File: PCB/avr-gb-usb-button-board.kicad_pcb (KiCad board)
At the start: 2 copper layers, 81 x 51.1 mm, 28 parts, among them IC1 ATTINY88-A

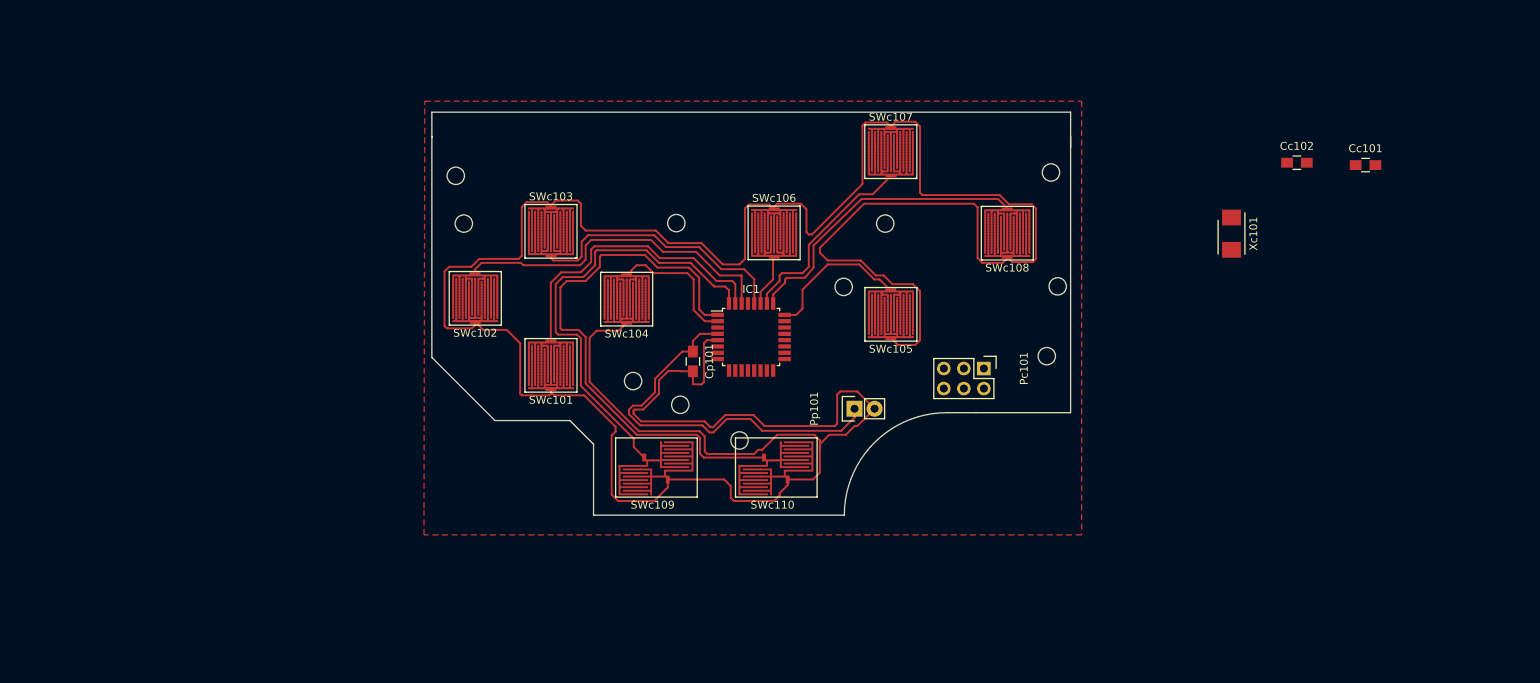
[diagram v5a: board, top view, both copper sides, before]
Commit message: Wired ISP header
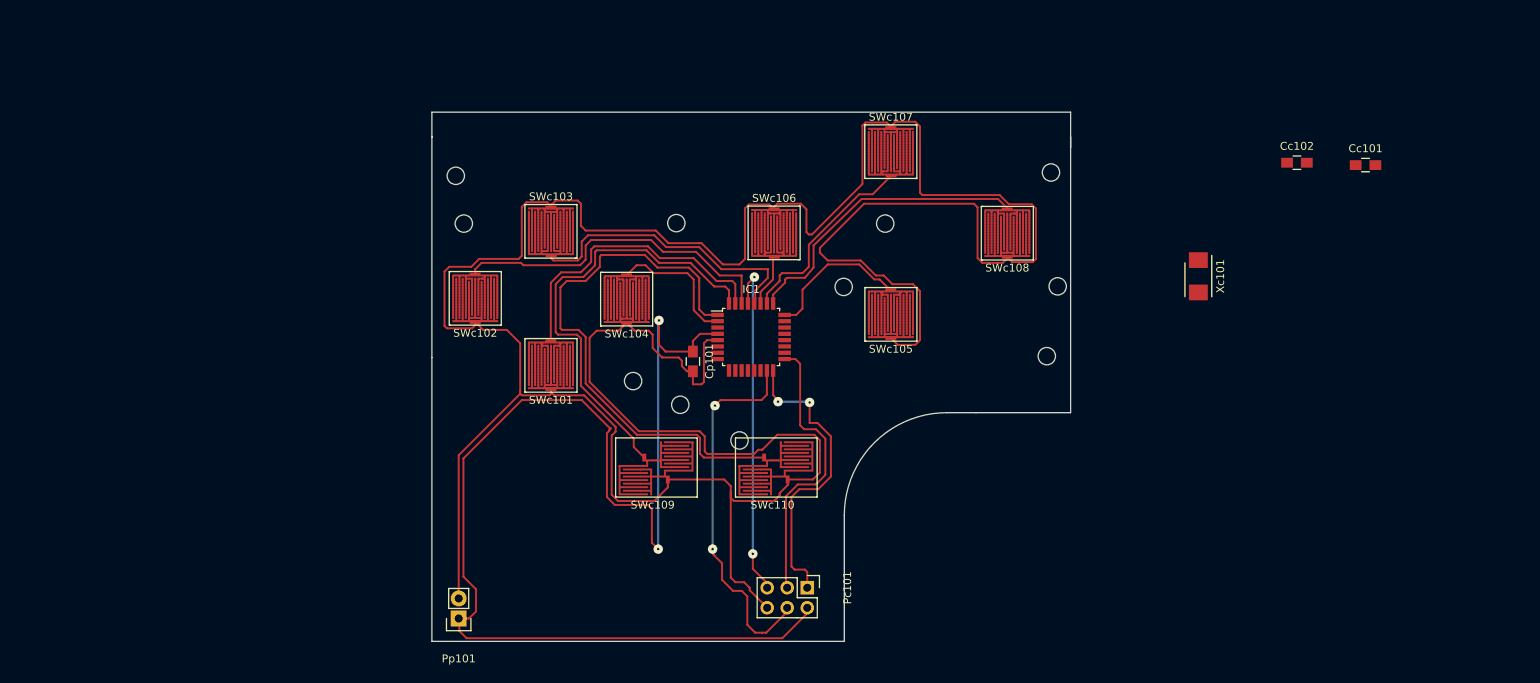
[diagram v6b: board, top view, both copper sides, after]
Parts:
- moved Pp101 56.8 mm to (22.8, 82.3), turned to 180 degrees
- moved Pc101 35.7 mm to (67.0, 78.4)
- moved Xc101 6.84 mm to (116.6, 38.9)
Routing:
- net VCC: track 50.3 -> 155.6 mm, vias 0 -> 2
- net Net-(IC1-Pad15): track 0.00 -> 47.7 mm, vias 0 -> 2
- net Net-(IC1-Pad29): track 0.00 -> 43.9 mm, vias 0 -> 2
- net Net-(IC1-Pad16): track 0.00 -> 38.5 mm, vias 0 -> 2
- net Net-(IC1-Pad17): track 0.00 -> 36.3 mm
- net Net-(IC1-Pad28): track 34.1 -> 37.3 mm
- net GND: track 389.2 -> 390.1 mm
- removed copper zone on F.Cu, net GND
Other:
- board size 81 x 51.1 mm -> 81 x 67.1 mm
- net class Default: via_dia 0.6 -> 1.2; via_drill 0.4 -> 0.3

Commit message: Added oscillator
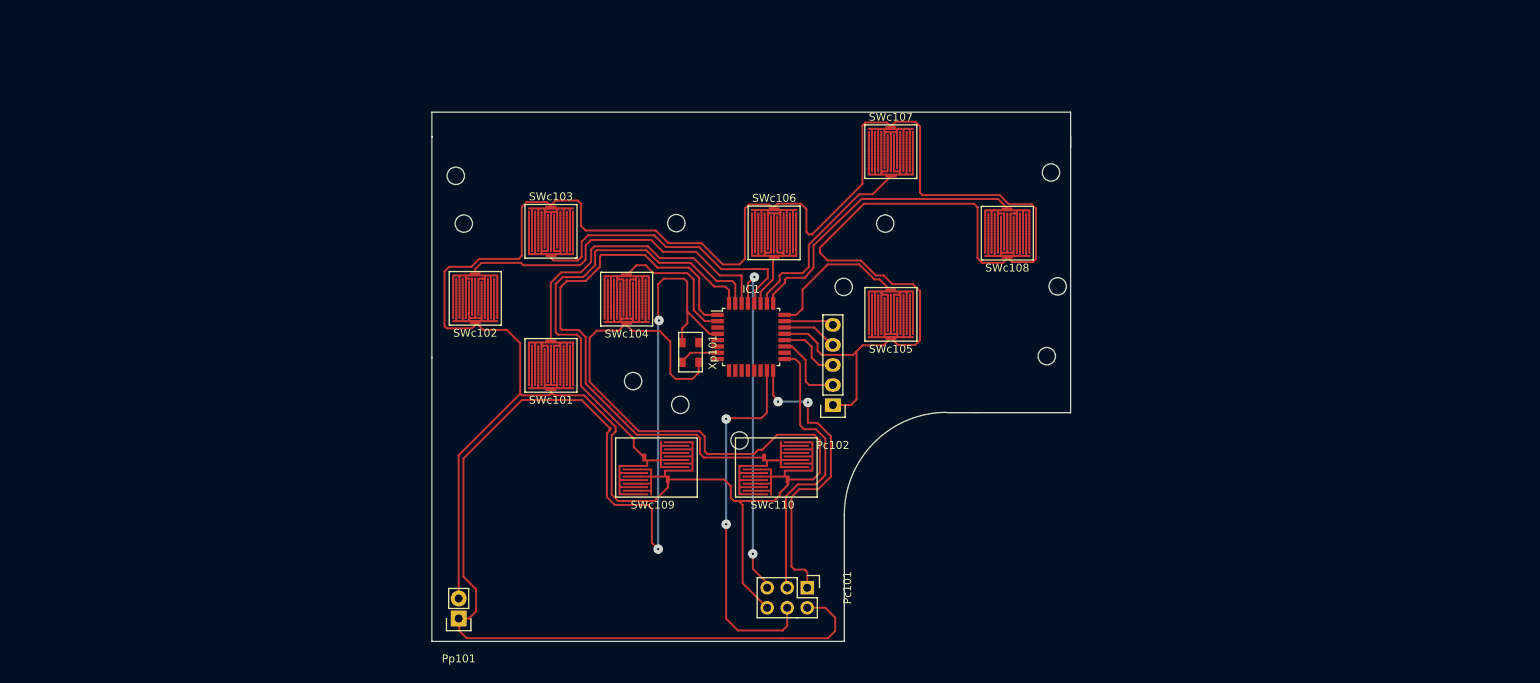
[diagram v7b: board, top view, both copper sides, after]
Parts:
- removed Cc101, Cc102: 22pF, Capacitors_SMD:C_0805_HandSoldering
- removed Cp101: 10uF, Capacitors_SMD:C_0805_HandSoldering
- removed Xc101: 12MHz, Crystals:Crystal_SMD_5032_2Pads
- added Pc102: CONN_01X05, Pin_Headers:Pin_Header_Straight_1x05, F.Cu at (70.2, 55.2)
- added Xp101: CRYSTAL_SMD, GBFootprints:KC5032A12.0000CMGE00, F.Cu at (52.2, 48.5)
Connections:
- IC1 pad 21: Net-(IC1-Pad21) -> GND
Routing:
- net VCC: track 155.6 -> 173.2 mm
- net GND: track 390.1 -> 407.3 mm
- net Net-(IC1-Pad19): track 0.00 -> 9.73 mm
- net Net-(IC1-Pad20): track 0.00 -> 8.23 mm
- net Net-(IC1-Pad22): track 0.00 -> 7.04 mm
- net Net-(IC1-Pad23): track 0.00 -> 6.31 mm
- net Net-(IC1-Pad7): track 0.00 -> 5.07 mm
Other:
- outline, holes or cut-outs redrawn

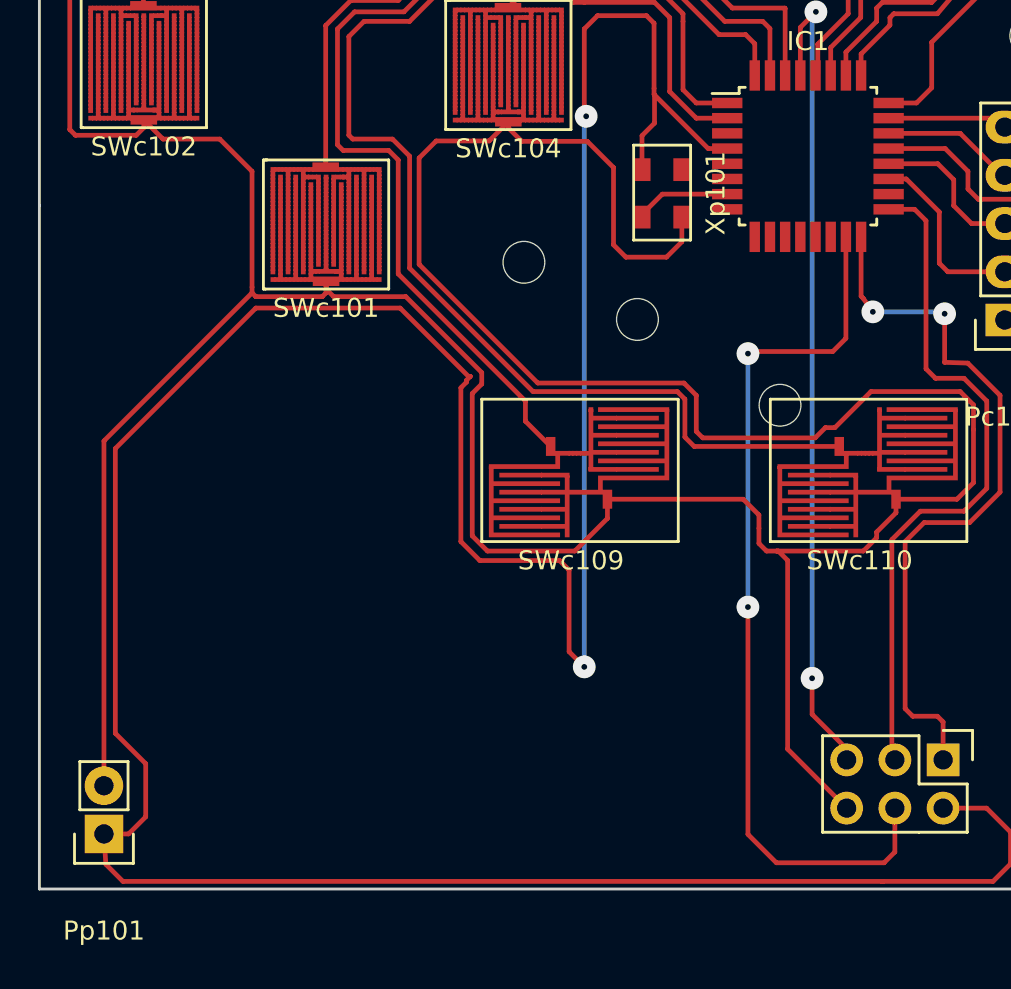
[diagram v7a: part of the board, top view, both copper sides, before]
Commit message: Added USB connector
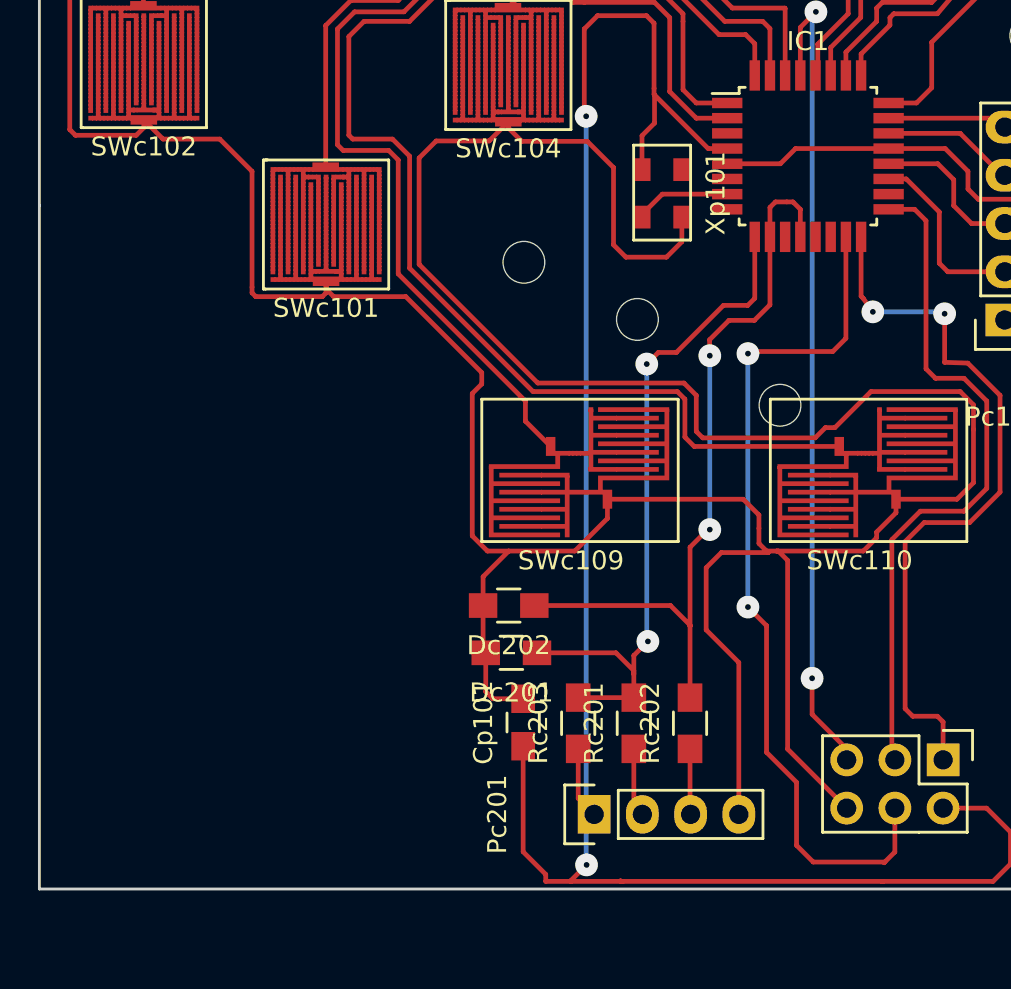
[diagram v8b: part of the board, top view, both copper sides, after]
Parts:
- removed Pp101: CONN_01X02, Pin_Headers:Pin_Header_Straight_1x02
- added Cp101: 10uF, Capacitors_SMD:C_0805_HandSoldering, F.Cu at (44.9, 76.4)
- added Dc201: 3V6, Resistors_SMD:R_0805_HandSoldering, F.Cu at (44.3, 72.8)
- added Dc202: 3V6, Resistors_SMD:R_0805_HandSoldering, F.Cu at (44.1, 70.3)
- added Pc201: CONN_01X04, Pin_Headers:Pin_Header_Straight_1x04, F.Cu at (48.6, 81.3)
- added Rc201: 47R, Resistors_SMD:R_0805_HandSoldering, F.Cu at (50.7, 76.5)
- added Rc202: 47R, Resistors_SMD:R_0805_HandSoldering, F.Cu at (53.7, 76.5)
- added Rc203: 2k, Resistors_SMD:R_0805_HandSoldering, F.Cu at (47.8, 76.5)
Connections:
- IC1 pad 10: Net-(IC1-Pad10) -> Net-(Dc202-Pad1)
- IC1 pad 12: Net-(IC1-Pad12) -> Net-(Dc202-Pad1)
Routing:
- net VCC: track 173.2 -> 104.8 mm
- net Net-(Dc202-Pad1): track 0.00 -> 40.4 mm, vias 0 -> 2
- net Net-(Dc201-Pad1): track 0.00 -> 36.9 mm, vias 0 -> 2
- net GND: track 407.3 -> 414.6 mm
- net Net-(Pc201-Pad2): track 0.00 -> 3.64 mm
- net Net-(Pc201-Pad3): track 0.00 -> 3.46 mm
- net Net-(IC1-Pad15): track 47.6 -> 46.4 mm
